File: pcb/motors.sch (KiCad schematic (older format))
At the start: 0 parts

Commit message: Fix Merges
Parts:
- added U? (x2): DRV8873SPWPRQ1, rasbot:DRV8873SPWPRQ1, symbol rasbot:DRV8873SPWPRQ1
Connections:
- new net: U?.16 (SRC), U?.17 (SRC) (x2)
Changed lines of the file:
@@
 EESchema Schematic File Version 4
 LIBS:rasbot-cache
-LIBS:inter-cache
 EELAYER 29 0
 EELAYER END
 $Descr A4 11693 8268
 encoding utf-8
-Sheet 1 13
+Sheet 12 13
 Title ""
 Date ""
@@
 Comment4 ""
 $EndDescr
+$Comp
+L rasbot:DRV8873SPWPRQ1 U?
+U 1 1 5D3E6DD6
+P 4450 3750
+F 0 "U?" H 4450 2861 50  0000 C CNN
+F 1 "DRV8873SPWPRQ1" H 4450 2770 50  0000 C CNN
+F 2 "rasbot:DRV8873SPWPRQ1" H 4450 2150 50  0001 C CNN
+F 3 "http://www.ti.com/lit/ds/symlink/drv8873.pdf" H 4450 4050 50  0001 C CNN
+	1    4450 3750
+	1    0    0    -1
+$EndComp
+$Comp
+L rasbot:DRV8873SPWPRQ1 U?
+U 1 1 5D3E7727
+P 6900 3750
+F 0 "U?" H 6900 2861 50  0000 C CNN
+F 1 "DRV8873SPWPRQ1" H 6900 2770 50  0000 C CNN
+F 2 "rasbot:DRV8873SPWPRQ1" H 6900 2150 50  0001 C CNN
+F 3 "http://www.ti.com/lit/ds/symlink/drv8873.pdf" H 6900 4050 50  0001 C CNN
+	1    6900 3750
+	1    0    0    -1
+$EndComp
 $EndSCHEMATC

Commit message: Fix and Anotate design
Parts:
- gave numbers to parts that had none: 2
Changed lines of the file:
@@
 EESchema Schematic File Version 4
-LIBS:rasbot-cache
 EELAYER 29 0
 EELAYER END
@@
 $EndDescr
 $Comp
-L rasbot:DRV8873SPWPRQ1 U?
+L rasbot:DRV8873SPWPRQ1 U58
 U 1 1 5D3E6DD6
 P 4450 3750
-F 0 "U?" H 4450 2861 50  0000 C CNN
+F 0 "U58" H 4450 2861 50  0000 C CNN
 F 1 "DRV8873SPWPRQ1" H 4450 2770 50  0000 C CNN
 F 2 "rasbot:DRV8873SPWPRQ1" H 4450 2150 50  0001 C CNN
@@
 $EndComp
 $Comp
-L rasbot:DRV8873SPWPRQ1 U?
+L rasbot:DRV8873SPWPRQ1 U59
 U 1 1 5D3E7727
 P 6900 3750
-F 0 "U?" H 6900 2861 50  0000 C CNN
+F 0 "U59" H 6900 2861 50  0000 C CNN
 F 1 "DRV8873SPWPRQ1" H 6900 2770 50  0000 C CNN
 F 2 "rasbot:DRV8873SPWPRQ1" H 6900 2150 50  0001 C CNN

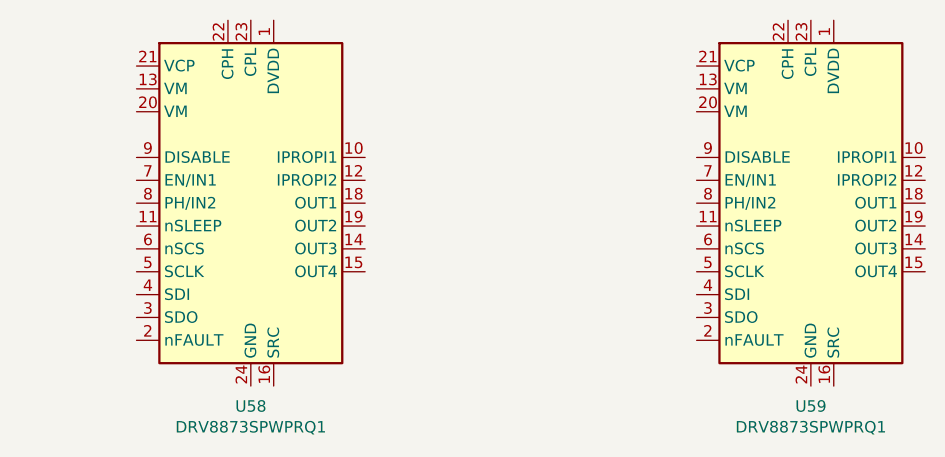
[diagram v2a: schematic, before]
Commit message: MCU connections, OLED and Sonar
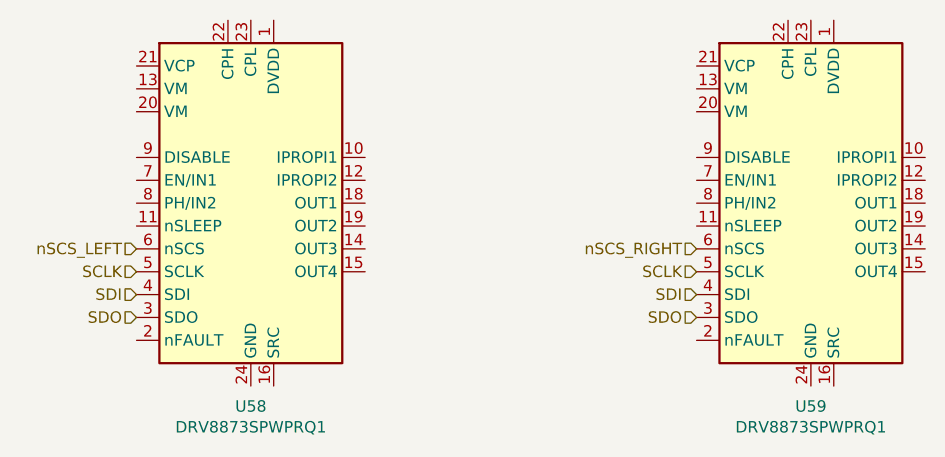
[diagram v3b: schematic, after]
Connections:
- net SDO: now reaches U58.3 (SDO)
- net SDO: now also U59.3 (SDO)
- net SDI: now reaches U58.4 (SDI)
- net SDI: now also U59.4 (SDI)
- net SCLK: now reaches U58.5 (SCLK)
- net SCLK: now also U59.5 (SCLK)
- net nSCS_LEFT: now reaches U58.6 (nSCS)
- net nSCS_RIGHT: now reaches U59.6 (nSCS)
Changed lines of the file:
@@
 	1    0    0    -1
 $EndComp
+Text HLabel 3950 4050 0    50   Input ~ 0
+SCLK
+Text HLabel 3950 4150 0    50   Input ~ 0
+SDI
+Text HLabel 3950 4250 0    50   Input ~ 0
+SDO
+Text HLabel 3950 3950 0    50   Input ~ 0
+nSCS_LEFT
+Text HLabel 6400 4050 0    50   Input ~ 0
+SCLK
+Text HLabel 6400 4150 0    50   Input ~ 0
+SDI
+Text HLabel 6400 4250 0    50   Input ~ 0
+SDO
+Text HLabel 6400 3950 0    50   Input ~ 0
+nSCS_RIGHT
 $EndSCHEMATC
